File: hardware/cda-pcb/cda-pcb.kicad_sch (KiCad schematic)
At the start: 194 parts, among them J1 ICD15S13E4GX00LF, J2 ICD15S13E4GX00LF, J3 ICD15S13E4GX00LF, J4 ICD15S13E4GX00LF, J5 Conn_01x06, P1 0022272021, U1 ADS124S08IRHBT, U10 SN74AHCT125RGYR, U2 ADS124S08IRHBT, U3 ADS124S08IRHBT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

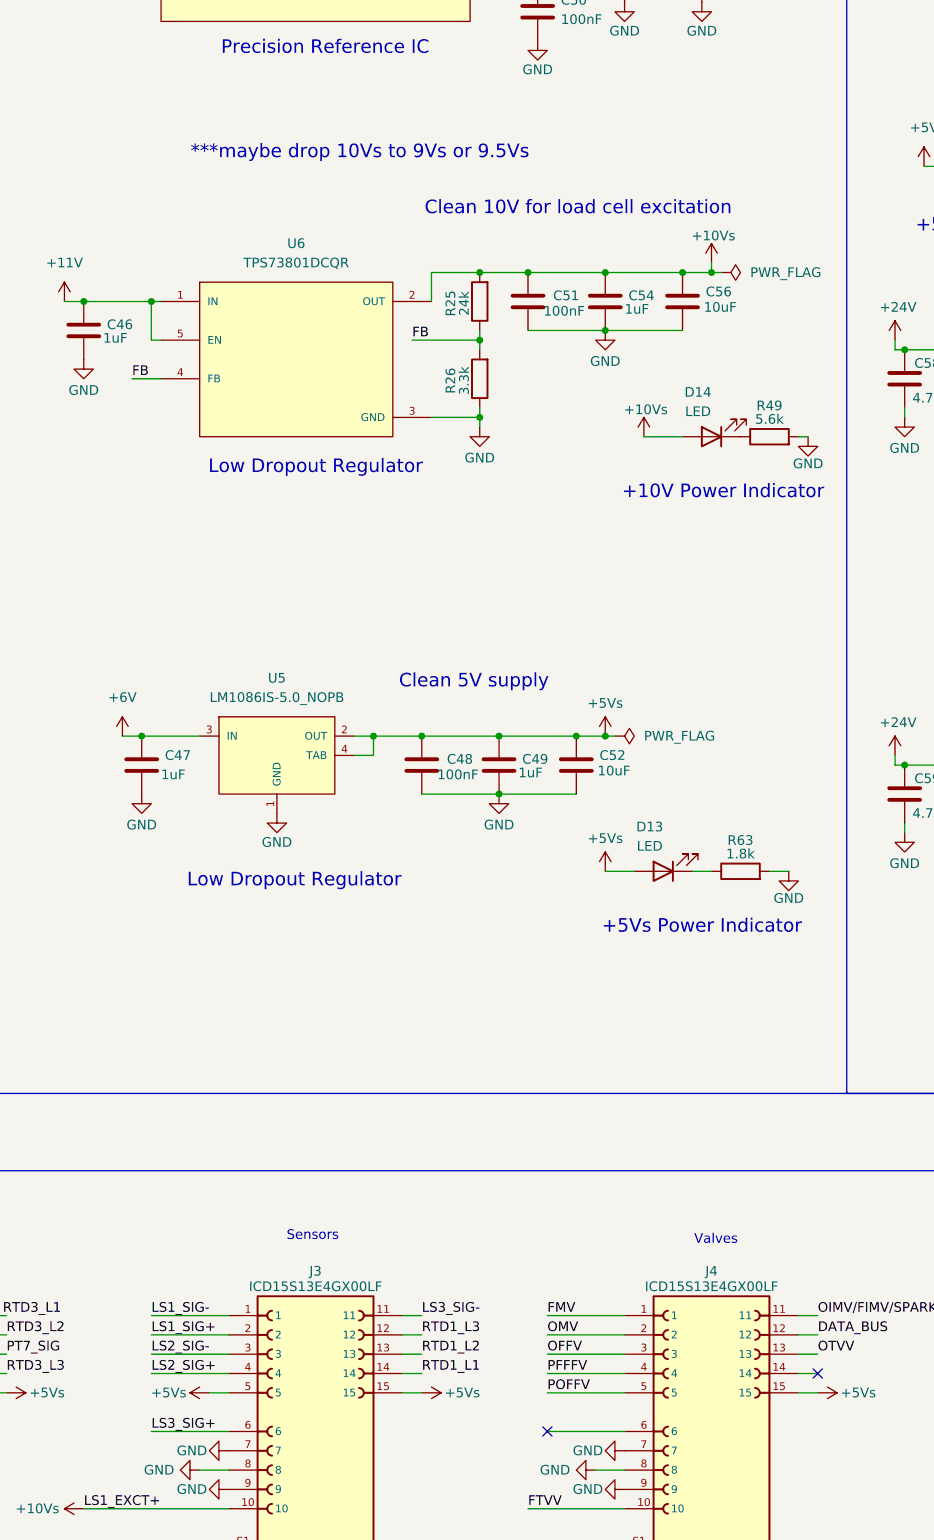
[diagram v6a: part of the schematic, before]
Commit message: changed 10Vs buck output to be 9.988V and added a 2nd 10Vs dsub pin
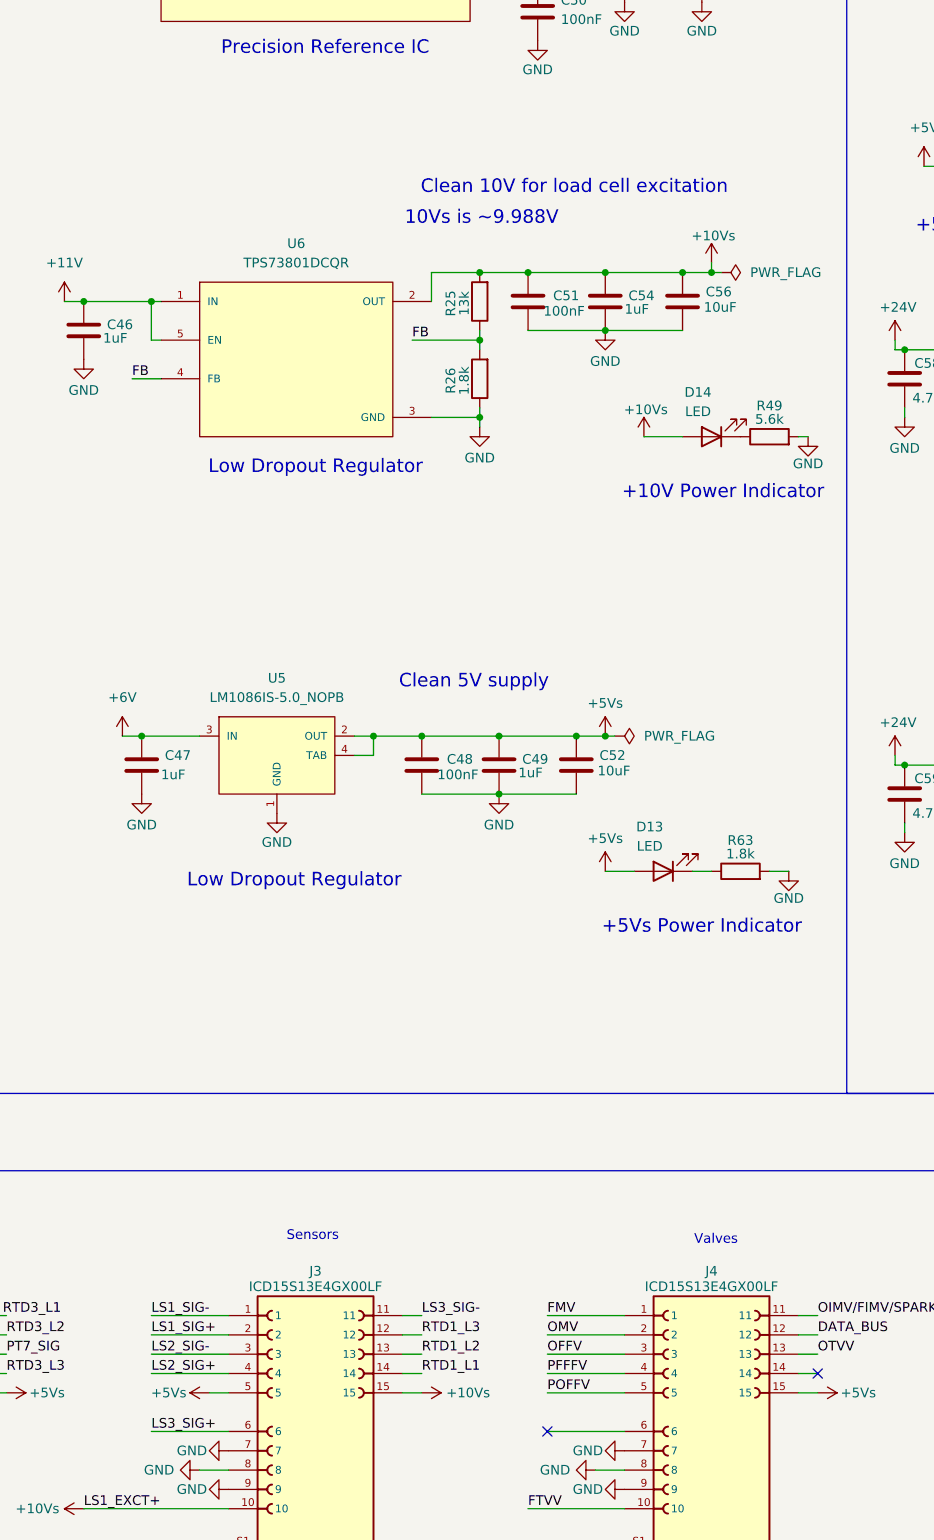
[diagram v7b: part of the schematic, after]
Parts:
- R25: value 24k -> 13k
- R26: value 3.3k -> 1.8k
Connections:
- net +10Vs: now also J3.15
- net +5Vs: no longer J3.15
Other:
- note added: "10Vs is ~9.988V"
- note removed: "***maybe drop 10Vs to 9Vs or 9.5Vs"
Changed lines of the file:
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@@
 		)
 	)
-	(text "***maybe drop 10Vs to 9Vs or 9.5Vs"
+	(text "10Vs is ~9.988V"
 		(exclude_from_sim no)
-		(at 391.922 191.262 0)
+		(at 407.924 199.898 0)
 		(effects
 			(font
@@
 	(text "Clean 10V for load cell excitation"
 		(exclude_from_sim no)
-		(at 420.624 198.628 0)
+		(at 420.116 195.834 0)
 		(effects
 			(font
@@
 			)
 		)
-		(property "Value" "3.3k"
+		(property "Value" "1.8k"
 			(at 405.638 221.234 90)
 			(effects
@@
 	)
 	(symbol
+		(lib_id "power:+9V")
+		(at 400.05 354.33 270)
+		(unit 1)
+		(exclude_from_sim no)
+		(in_bom yes)
+		(on_board yes)
+		(dnp no)
+		(property "Reference" "#PWR0186"
+			(at 396.24 354.33 0)
+			(effects
+				(font
+					(size 1.27 1.27)
+				)
+				(hide yes)
+			)
+		)
+		(property "Value" "+10Vs"
+			(at 406.146 354.33 90)
+			(effects
+				(font
+					(size 1.27 1.27)
+				)
+			)
+		)
+		(property "Footprint" ""
+			(at 400.05 354.33 0)
+			(effects
+				(font
+					(size 1.27 1.27)
+				)
+				(hide yes)
+			)
+		)
+		(property "Datasheet" ""
+			(at 400.05 354.33 0)
+			(effects
+				(font
+					(size 1.27 1.27)
+				)
+				(hide yes)
+			)
+		)
+		(property "Description" "Power symbol creates a global label with name \"+9V\""
+			(at 400.05 354.33 0)
+			(effects
+				(font
+					(size 1.27 1.27)
+				)
+				(hide yes)
+			)
+		)
+		(pin "1"
+		)
+		(instances
+			(project "cda-pcb"
+				(path "/98ce85a8-ddff-4ecb-9668-dd271ba07a43"
+					(reference "#PWR0186")
+					(unit 1)
+				)
+			)
+		)
+	)
+	(symbol
 		(lib_id "Device:R")
 		(at 57.15 234.95 90)
@@
 			)
 		)
-		(property "Value" "24k"
+		(property "Value" "13k"
 			(at 405.638 211.074 90)
 			(effects
@@
 					(unit 1)
 				)
-			)
-		)
-	)
-	(symbol
-		(lib_id "power:+5V")
-		(at 400.05 354.33 270)
-		(unit 1)
-		(exclude_from_sim no)
-		(in_bom yes)
-		(on_board yes)
-		(dnp no)
-		(property "Reference" "#PWR032"
-			(at 396.24 354.33 0)
-			(effects
-				(font
-					(size 1.27 1.27)
-				)
-				(hide yes)
-			)
-		)
-		(property "Value" "+5Vs"
-			(at 405.384 354.33 90)
-			(effects
-				(font
-					(size 1.27 1.27)
-				)
-			)
-		)
-		(property "Footprint" ""
-			(at 400.05 354.33 0)
-			(effects
-				(font
-					(size 1.27 1.27)
-				)
-				(hide yes)
-			)
-		)
-		(property "Datasheet" ""
-			(at 400.05 354.33 0)
-			(effects
-				(font
-					(size 1.27 1.27)
-				)
-				(hide yes)
-			)
-		)
-		(property "Description" "Power symbol creates a global label with name \"+5V\""
-			(at 400.05 354.33 0)
-			(effects
-				(font
-					(size 1.27 1.27)
-				)
-				(hide yes)
-			)
-		)
-		(pin "1"
-		)
-		(instances
-			(project "DAQ"
-				(path "/98ce85a8-ddff-4ecb-9668-dd271ba07a43"
-					(reference "#PWR032")
-					(unit 1)
-				)

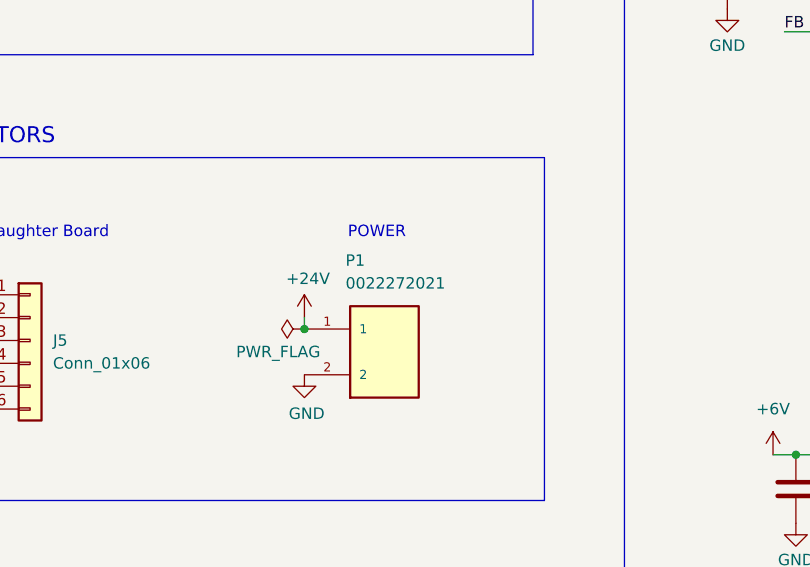
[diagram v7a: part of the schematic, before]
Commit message: finished back soldermask, re-added stitching vias, made gerbs
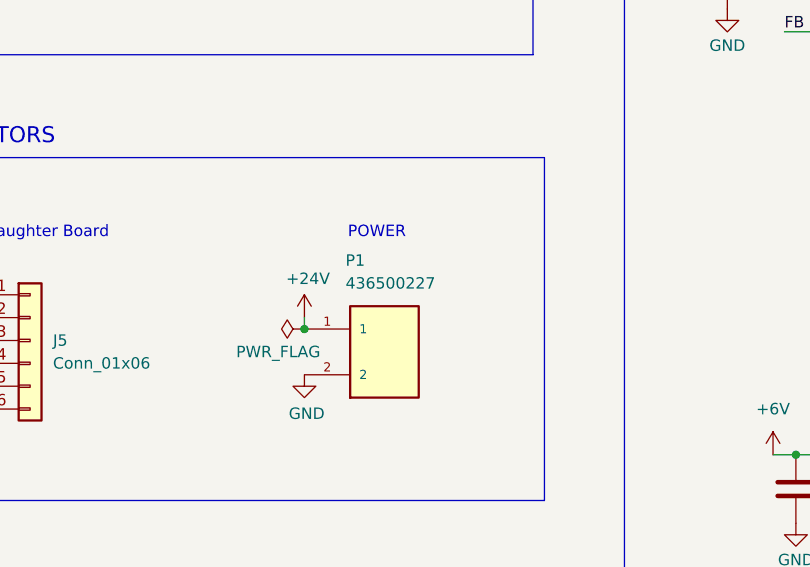
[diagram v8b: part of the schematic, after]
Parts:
- P1: value 0022272021 -> 436500227; footprint 0022272021:MOLEX_0022272021 -> molex_microfit_3.0:CONN_SD-43650-010_02_MOL
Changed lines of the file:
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@@
 			)
 		)
-		(property "Value" "0022272021"
+		(property "Value" "436500227"
 			(at 313.182 248.92 0)
 			(effects
@@
 			)
 		)
-		(property "Footprint" "0022272021:MOLEX_0022272021"
+		(property "Footprint" "molex_microfit_3.0:CONN_SD-43650-010_02_MOL"
 			(at 313.69 256.54 0)
 			(effects
